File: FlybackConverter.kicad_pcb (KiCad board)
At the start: 2 copper layers, 50.8 x 50.8 mm, 32 parts, among them J1 USB_A, T1 Transformer_1P_2S, U1 LNK6428K

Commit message: 仮配置
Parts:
- removed D4: D_Schottky, Diode_SMD:D_PowerDI-5
- added FL1: TestPoint, TestPoint:TestPoint_Loop_D1.80mm_Drill1.0mm_Beaded, F.Cu at (181.9, 58.8)
- added FL2: TestPoint, TestPoint:TestPoint_Loop_D1.80mm_Drill1.0mm_Beaded, F.Cu at (181.9, 66.8)
- added REF**: MountingHole_3.2mm_M3, MountingHole:MountingHole_3.2mm_M3, F.Cu at (199.6, 123.4)
- added REF**: MountingHole_3.2mm_M3, MountingHole:MountingHole_3.2mm_M3, F.Cu at (130.6, 123.4)
- added REF**: MountingHole_3.2mm_M3, MountingHole:MountingHole_3.2mm_M3, F.Cu at (199.6, 54.4)
- added REF**: MountingHole_3.2mm_M3, MountingHole:MountingHole_3.2mm_M3, F.Cu at (130.6, 54.4)
- BR1, C5, C6, C7, C8, D1, D2, D3, R1, R10, R11, R2, R3, R5, R7, R8, U1: moved to B.Cu
- R6: value 14.8k -> 42.2; moved to B.Cu
- moved T1 137.9 mm to (177.8, 94.9), turned to 90 degrees
- moved D1 135.4 mm to (189.1, 63.2), turned to 180 degrees
- moved J1 123.7 mm to (189.7, 111.1), turned to 90 degrees
- moved L1 121.6 mm to (197.4, 78.0), turned to -90 degrees
- moved C4 119.9 mm to (191.1, 85.1), turned to 180 degrees
- moved C3 119.7 mm to (191.1, 74.9), turned to 180 degrees
- moved C1 118.4 mm to (158.6, 103.4), turned to 180 degrees
- moved RT1 111.4 mm to (147.0, 109.0), turned to 180 degrees
- moved R3 107.5 mm to (176.8, 100.6)
- moved BR1 104.2 mm to (155.7, 112.3), turned to 180 degrees
- moved D2 101.2 mm to (177.0, 96.8), turned to 180 degrees
- moved R11 100.0 mm to (169.7, 100.6)
- moved R2 98.7 mm to (192.5, 107.7), turned to 90 degrees
- moved C5 98.2 mm to (191.6, 58.8)
- moved R1 96.3 mm to (187.3, 58.8), turned to 180 degrees
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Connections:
- C2 pad 2: Net-(T1-SC) -> Net-(T1-SB)
- C3 pad 2: Net-(J1-GND) -> FL2
- C4 pad 2: Net-(J1-GND) -> FL2
- C7 pad 2: Net-(T1-SC) -> Net-(T1-SB)
- C8 pad 2: Net-(T1-SC) -> Net-(T1-SB)
- D1 pad 2: Net-(D1-A) -> FL1
- J1 pad 4: Net-(J1-GND) -> FL2
- J1 pad 5: Net-(J1-GND) -> FL2
- L3 pad 2: Net-(T1-SC) -> Net-(T1-SB)
- R1 pad 2: Net-(D1-A) -> FL1
- R2 pad 2: Net-(J1-GND) -> FL2
- R5 pad 1: Net-(T1-SD) -> Net-(T1-SA)
- R6 pad 1: Net-(T1-SD) -> Net-(T1-SA)
- R7 pad 2: Net-(T1-SC) -> Net-(T1-SB)
- T1 pad 1: Net-(T1-AA) -> (no net)
- T1 pad 2: Net-(D2-A) -> (no net)
- T1 pad 3: Net-(D1-A) -> Net-(T1-SA)
- T1 pad 4: Net-(J1-GND) -> Net-(T1-SB)
- T1 pad 5: Net-(T1-SC) -> Net-(T1-AA)
- T1 pad 6: Net-(T1-SD) -> Net-(D2-A)
- U1 pad 10: Net-(T1-SC) -> Net-(T1-SB)
- U1 pad 11: Net-(T1-SC) -> Net-(T1-SB)
- U1 pad 12: Net-(T1-SC) -> Net-(T1-SB)
- U1 pad 13: (no net) -> Net-(T1-SB)
- U1 pad 3: (no net) -> Net-(T1-SB)
- U1 pad 4: (no net) -> Net-(T1-SB)
- U1 pad 7: Net-(T1-SC) -> Net-(T1-SB)
- U1 pad 8: Net-(T1-SC) -> Net-(T1-SB)
- U1 pad 9: Net-(T1-SC) -> Net-(T1-SB)
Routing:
- net FL2: track 0.00 -> 65.1 mm
- net Net-(J1-VBUS): track 0.00 -> 39.2 mm
- net Net-(D2-A): track 0.00 -> 32.8 mm
- net Net-(BR1-+): track 0.00 -> 28.4 mm
- net Net-(BR1--): track 0.00 -> 25.8 mm
- net Net-(D1-K): track 0.00 -> 25.0 mm
- net Net-(T1-SA): track 0.00 -> 12.4 mm
- net Net-(RT1-Pad2): track 0.00 -> 11.9 mm
- net Net-(U1-BP): track 0.00 -> 10.1 mm
- net FL1: track 0.00 -> 9.75 mm
- net Net-(F1-Pad2): track 0.00 -> 8.67 mm
- net Net-(D3-K): track 0.00 -> 8.13 mm
- net Net-(C6-Pad2): track 0.00 -> 8.06 mm
- net Net-(U1-FB): track 0.00 -> 7.76 mm
- net Net-(BR1-Pad3): track 0.00 -> 6.75 mm
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- added copper zone on B.Cu, net Net-(T1-AA)
- added copper zone on B.Cu, net Net-(T1-SB)
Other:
- board size 50.8 x 50.8 mm -> 76.2 x 76.2 mm

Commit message: TypeC仮配置 #1
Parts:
- added R4: 100k, Resistor_SMD:R_0603_1608Metric, F.Cu at (212.5, 99.8)
- added U2: TPS25820DSST, 00_Library:TPS25820, B.Cu at (192.8, 104.1)
- J1: value USB_A -> USB_C_Receptacle_PowerOnly_6P; footprint Connector_USB:USB_A_CONNFLY_DS1095-WNR0 -> 00_Library:USB-C-SMD_TYPE-C-6P
- moved J1 9.04 mm to (198.5, 113.5)
- moved R2 8.34 mm to (190.7, 99.6), turned to 180 degrees
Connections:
- C4 pad 1: Net-(J1-VBUS) -> 5V
- L1 pad 2: Net-(J1-VBUS) -> 5V
- R2 pad 1: Net-(J1-VBUS) -> 5V
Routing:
- net Net-(J1-VBUS): track 39.2 -> 0.00 mm
- net FL2: track 65.1 -> 41.0 mm
- net 5V: track 0.00 -> 19.8 mm

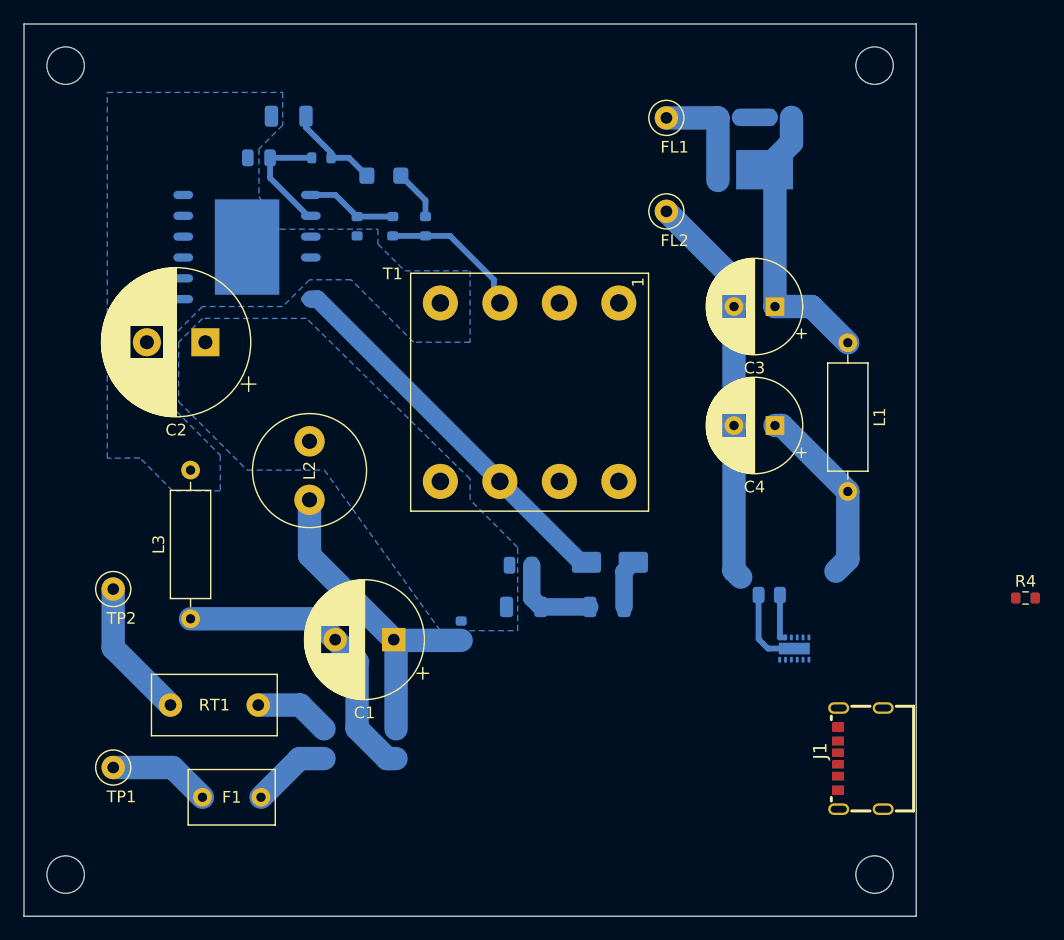
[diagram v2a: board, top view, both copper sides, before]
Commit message: USBコントローラ配置 #1
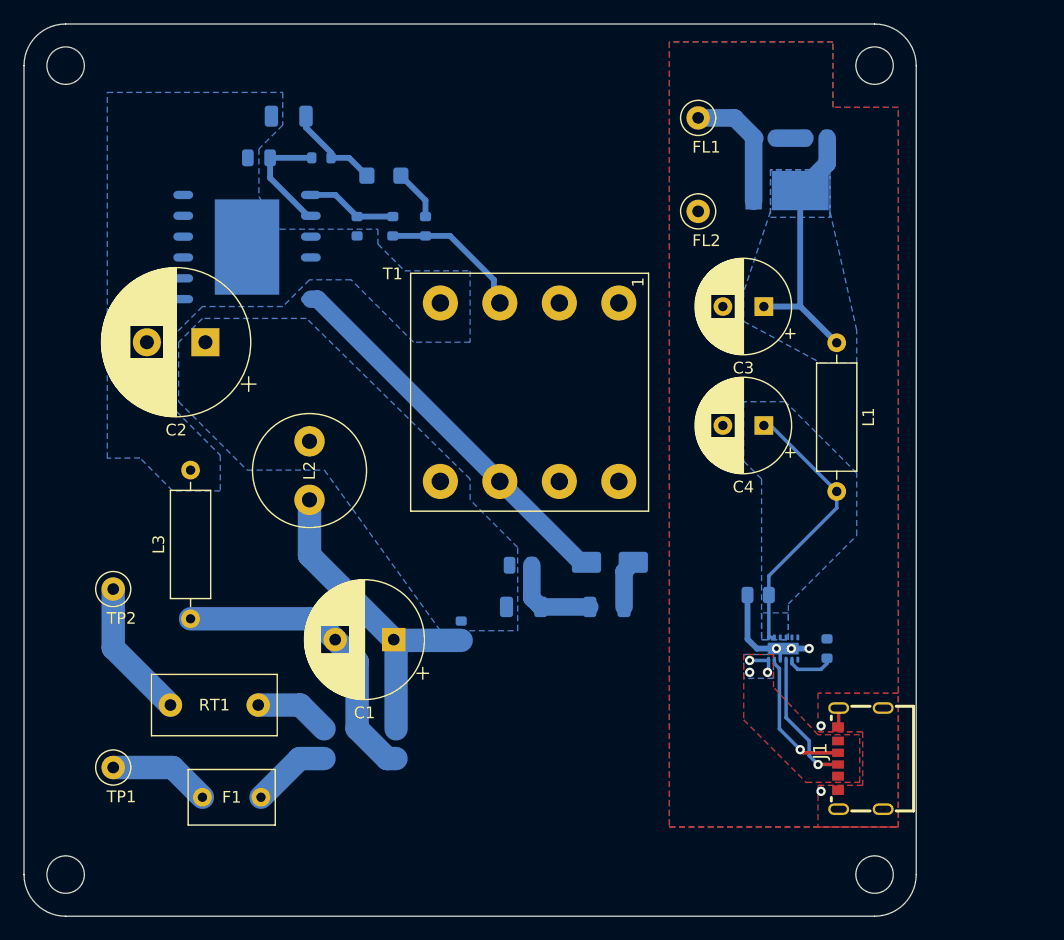
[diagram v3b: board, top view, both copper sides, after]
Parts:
- R4: moved to B.Cu
- moved R4 17.5 mm to (195.6, 104.1), turned to 90 degrees
- moved D1 3.53 mm to (192.2, 65.0)
- moved R1 3.53 mm to (190.3, 60.5)
- moved C5 3.53 mm to (194.6, 60.5)
- moved FL1 2.71 mm to (184.6, 58.8)
- moved FL2 2.71 mm to (184.6, 66.8)
- moved C3 0.95 mm to (190.2, 74.9)
- moved C4 0.95 mm to (190.2, 85.1)
- moved L1 0.95 mm to (196.4, 78.0)
- moved R2 0.95 mm to (189.7, 99.6)
- moved U2 0.95 mm to (191.8, 104.1)
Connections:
- U2 pad 10: (no net) -> FL2
- U2 pad 3: FL2 -> 5V
- U2 pad 4: (no net) -> 5V
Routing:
- net FL2: track 41.0 -> 12.3 mm, vias 0 -> 5
- net Net-(J1-CC2): track 0.00 -> 11.9 mm, vias 0 -> 1
- net Net-(J1-CC1): track 0.00 -> 11.8 mm, vias 0 -> 1
- net Net-(U2-REF): track 0.00 -> 4.19 mm
- net 5V: track 19.8 -> 23.8 mm
- net VBUS: track 0.00 -> 2.76 mm, vias 0 -> 3
- net Net-(D1-K): track 25.0 -> 22.8 mm
- net FL1: track 9.75 -> 10.9 mm
- added copper zone on B.Cu, net 5V
- added copper zone on B.Cu, net FL2
- added copper zone on F.Cu, net FL2
- added copper zone on B.Cu, net Net-(D1-K)
- added copper zone on B.Cu, net VBUS
- added copper zone on F.Cu, net VBUS
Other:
- outline, holes or cut-outs redrawn

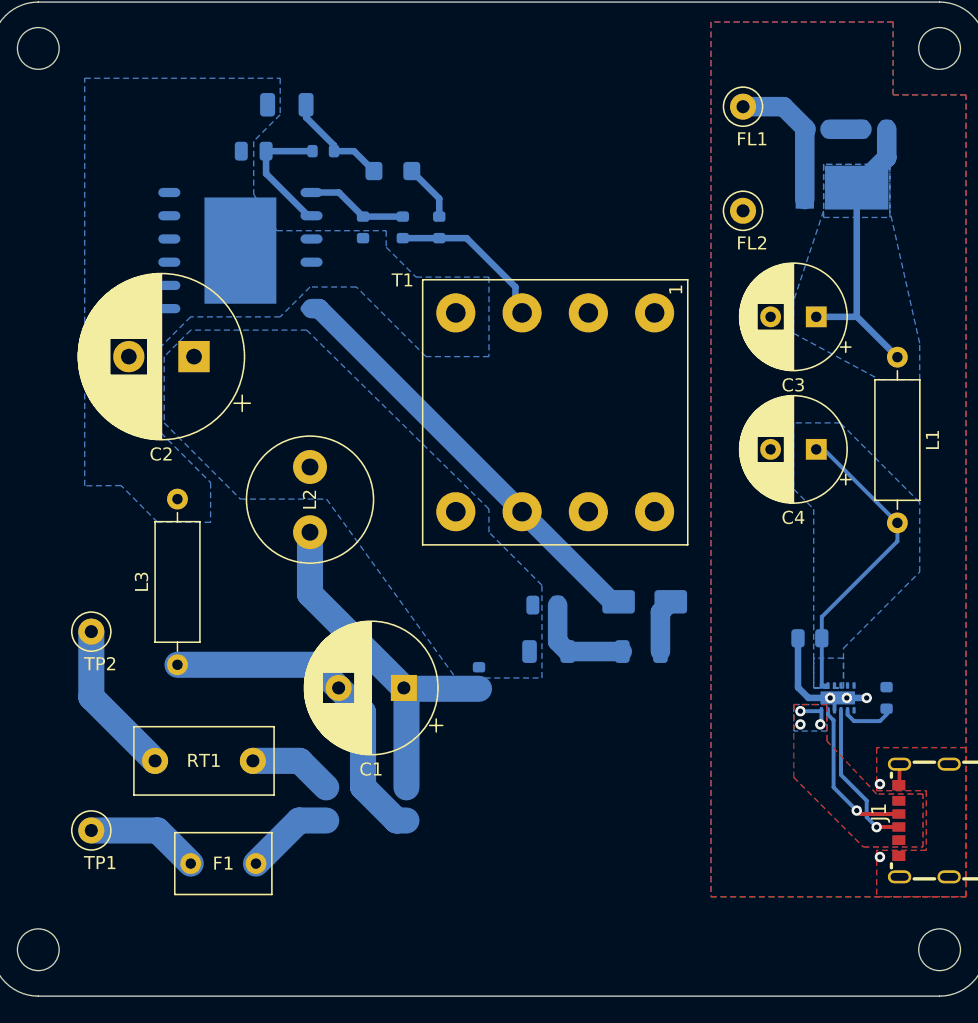
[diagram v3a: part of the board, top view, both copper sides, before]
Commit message: AC側配線幅1mmで統一 fix #4
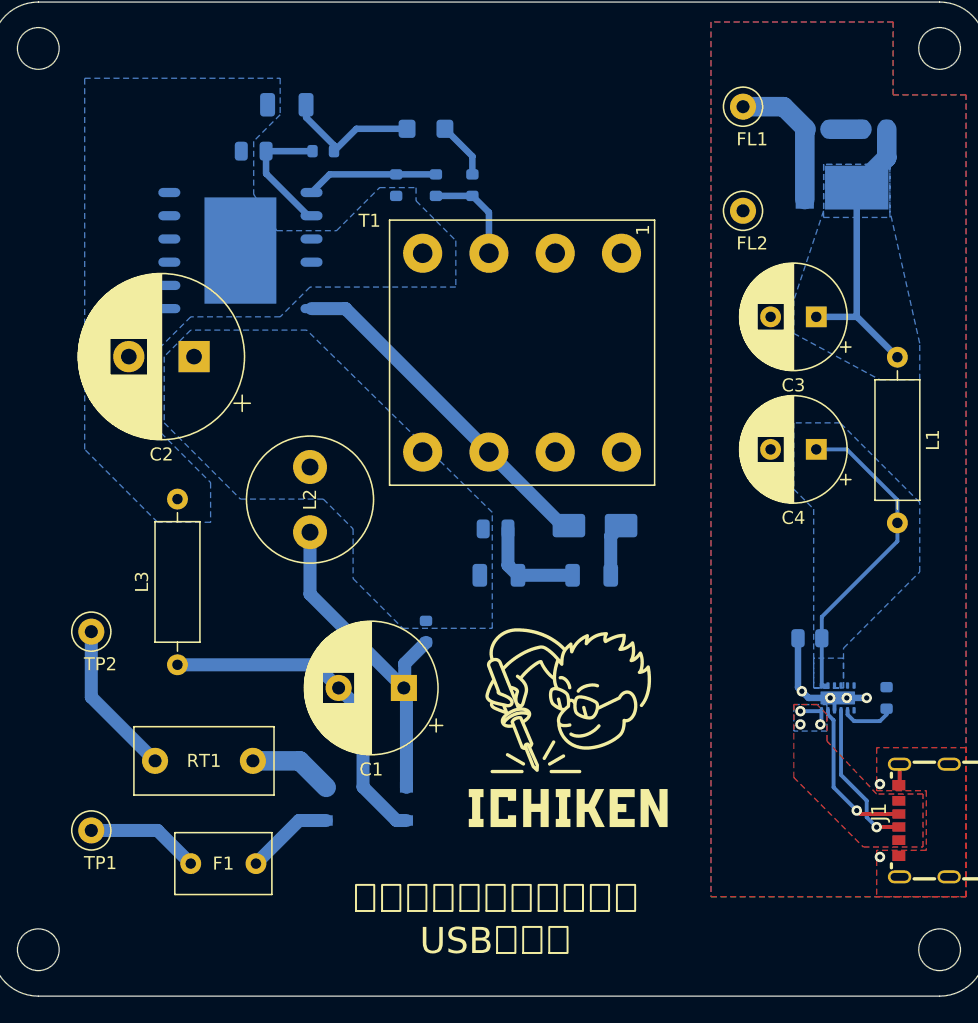
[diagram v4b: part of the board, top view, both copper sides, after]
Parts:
- moved C6 6.97 mm to (165.6, 91.2)
- moved D2 6.97 mm to (173.2, 90.9)
- moved R11 6.97 mm to (165.9, 94.7)
- moved R3 6.97 mm to (173.0, 94.7)
- moved R10 5.40 mm to (160.3, 99.1)
- moved T1 5.23 mm to (175.3, 90.4)
- moved R5 4.12 mm to (163.8, 64.8)
- moved R6 4.12 mm to (161.0, 64.8)
- moved R7 4.12 mm to (158.0, 64.8)
- moved D3 4.12 mm to (160.3, 60.5)
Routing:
- net Net-(D2-A): track 32.8 -> 26.6 mm
- net Net-(T1-SA): track 12.4 -> 7.72 mm
- net Net-(D3-K): track 8.13 -> 10.8 mm
- net Net-(U1-FB): track 7.76 -> 10.1 mm
- net Net-(BR1-+): track 28.4 -> 26.9 mm
- net 5V: track 23.8 -> 24.8 mm
- net FL2: vias 5 -> 6
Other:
- board text added: "フライバックコンバータ USB充電器"
